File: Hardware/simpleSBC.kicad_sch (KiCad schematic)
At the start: 56 parts, among them J1 Conn_02x07_Odd_Even, J3 Conn_01x06_Male, J5 USB_A, J6 USB_A, J7 RJ45_Wuerth_7499010121A, U1 STM32MP157FAD1, U2 STMPS2252MTR, U5 USBLC6-4SC6, U6 LAN8742A, X1 ASCO, Y1 32.786, Y2 X53T-C20SSA-25.000MHz

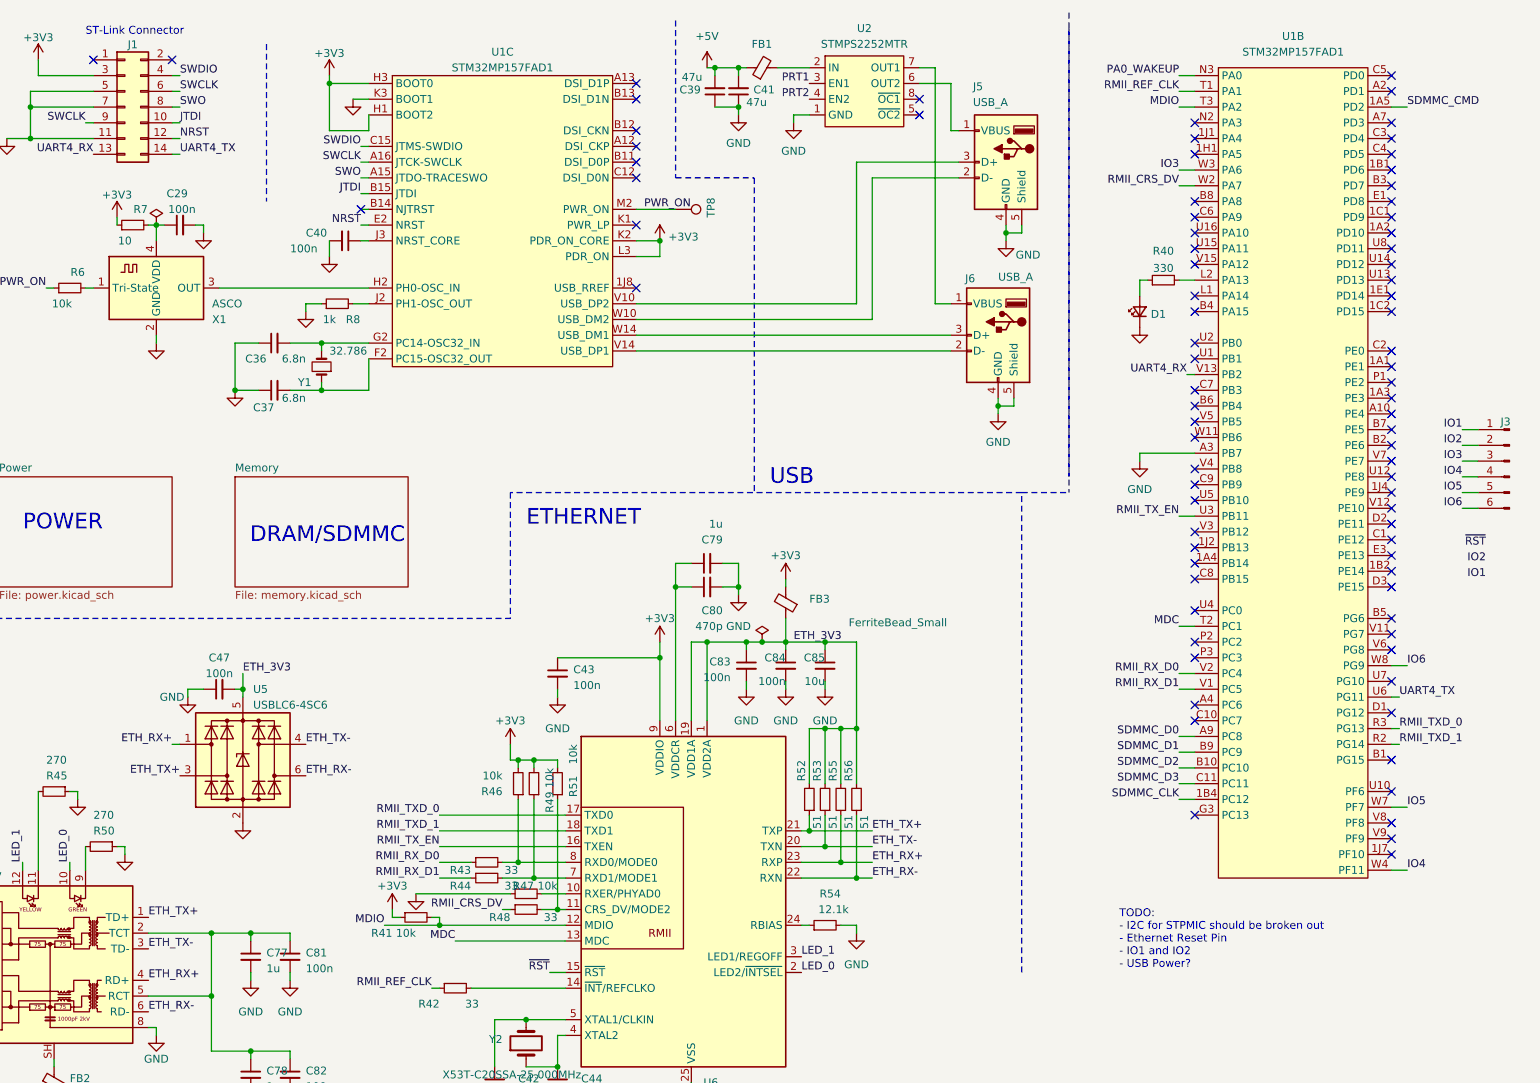
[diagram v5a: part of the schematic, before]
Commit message: Schematic symbol pin type fixes
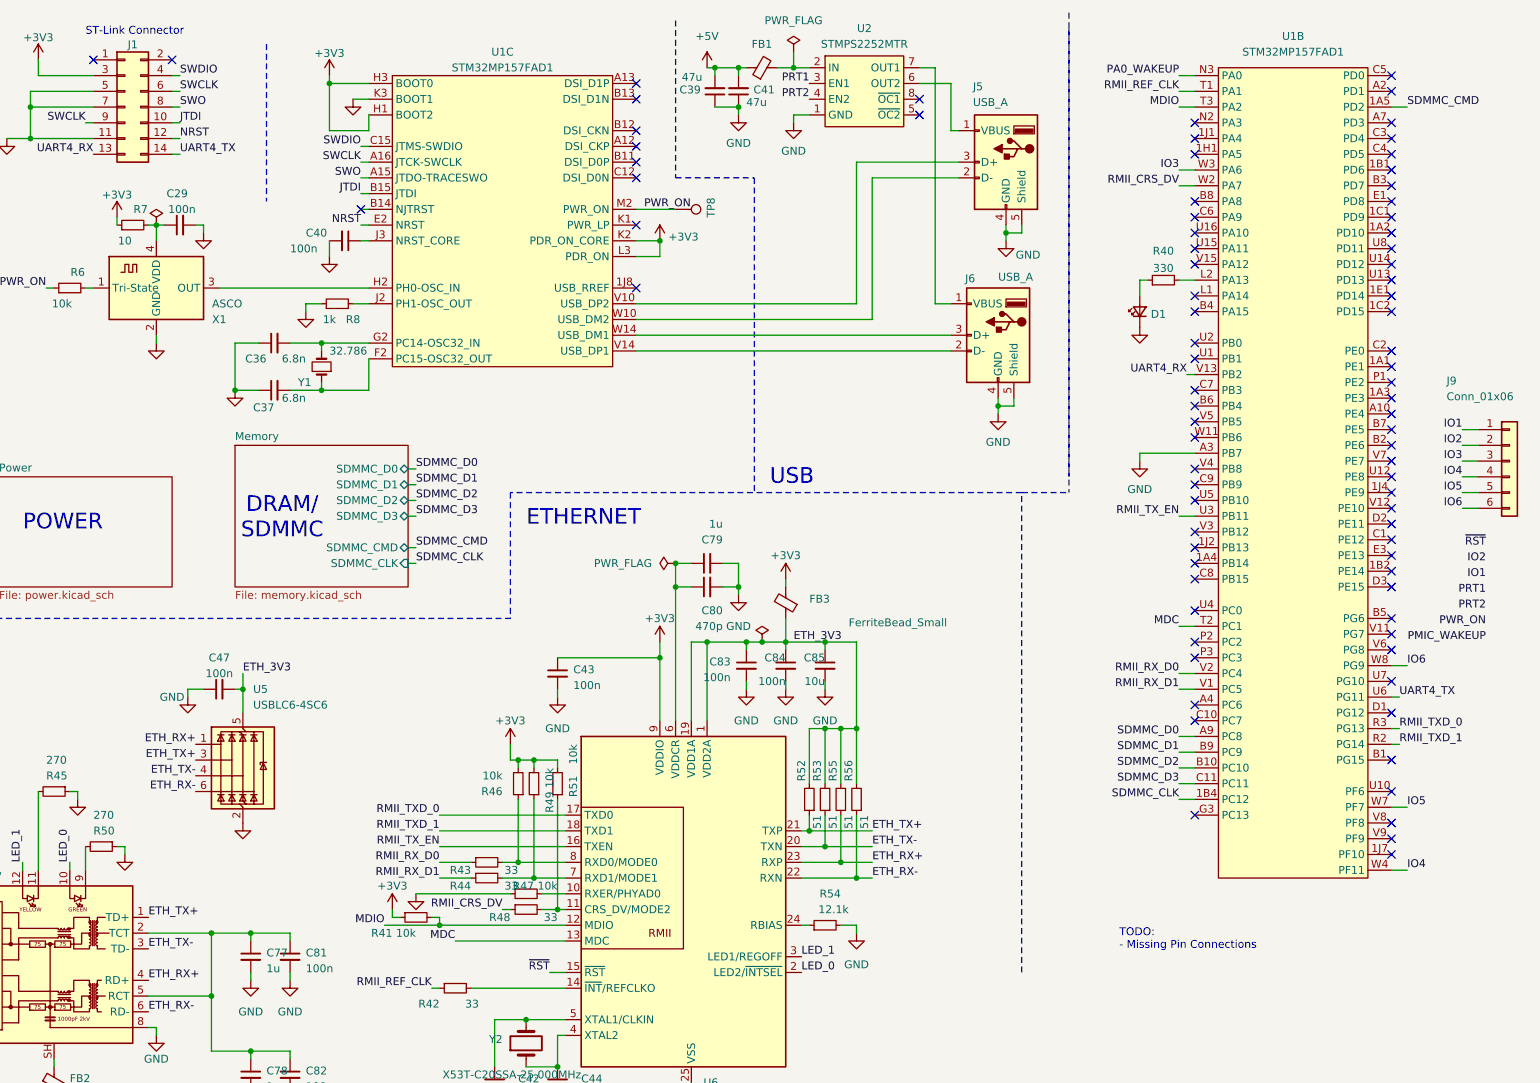
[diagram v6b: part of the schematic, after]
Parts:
- removed J3: Conn_01x06_Male, Connector_PinHeader_2.54mm:PinHeader_1x06_P2.54mm_Vertical, symbol Connector:Conn_01x06_Male
- added J9: Conn_01x06, Connector_PinHeader_2.54mm:PinHeader_1x06_P2.54mm_Vertical, symbol Connector_Generic:Conn_01x06
- FB1: footprint (none) -> Inductor_SMD:L_0603_1608Metric
- J1: footprint personal:PinHeader_2x7_P1.27mm_SMD -> SimpleSBC:PinHeader_2x7_P1.27mm_SMD
- R41, R42, R43, R44, R45, R46, R47, R48, R49, R50, R51, R52, R53, R54, R55, R56: footprint Resistor_SMD:R_0603_1608Metric -> Resistor_SMD:R_0402_1005Metric
- TP8: footprint personal:PROBE_PAD_1206 -> TestPoint:TestPoint_Pad_D1.0mm
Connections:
- net IO1: now also J9.1 (Pin_1)
- net IO2: now also J9.2 (Pin_2)
- net IO3: now also J9.3 (Pin_3)
- net IO4: now also J9.4 (Pin_4)
- net IO5: now also J9.5 (Pin_5)
- net IO6: now also J9.6 (Pin_6)
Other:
- sheet Memory ports: added SDMMC_CLK, SDMMC_CMD, SDMMC_D0, SDMMC_D1, SDMMC_D2, SDMMC_D3; removed none
- note added: "DRAM/ SDMMC"
- note added: "TODO: - Missing Pin Connections"
- note removed: "DRAM/SDMMC"
- note removed: "TODO: - I2C for STPMIC should be broken out - Ethernet Reset Pin - IO1 and IO2 - USB Power?"

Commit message: First pass through ST Design Checklist
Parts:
- removed FB2: FerriteBead_Small, Inductor_SMD:L_0603_1608Metric, symbol Device:FerriteBead_Small
- added C97: 10n, Capacitor_SMD:C_0402_1005Metric, symbol Device:C_Small
- added D2: LED_Small, LED_SMD:LED_0805_2012Metric, symbol Device:LED_Small
- added JP1: SolderJumper_2_Bridged, symbol Jumper:SolderJumper_2_Bridged
- added R60: 10k, Resistor_SMD:R_0402_1005Metric, symbol Device:R_Small
- added R61: 330, Resistor_SMD:R_0402_1005Metric, symbol Device:R_Small
- added R62: 3k, Resistor_SMD:R_0402_1005Metric, symbol Device:R_Small
- C40: value 100n -> 10n
- C42, C43, C44, C47, C77, C78, C79, C80, C81, C82, C83, C84: footprint Capacitor_SMD:C_0603_1608Metric -> Capacitor_SMD:C_0402_1005Metric
- R8: value 1k -> 470
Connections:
- net +3V3: now also C77.1, C78.1, C81.1, C82.1, J7.2 (TCT), J7.5 (RCT), R60.2
- net GND: now also C97.2, D2.1 (K), R62.1
- net NRST: now also C97.1, JP1.2 (B)
- net UART4_RX: now also R60.1
- net ~{RST}: no longer U6.15 (~{RST})
- net RTC_OUT1: now reaches U1.G3 (PC13)
- net at U1.L1 (PA14): now also R61.2
- net I2C4_SDA: now reaches U1.U13 (PD13)
- net I2C4_SCL: now reaches U1.U14 (PD12)
- net at U1.1J8 (USB_RREF): now also R62.2
- new net: D2.2 (A), R61.1
- new net Power/~{RST}: JP1.1 (A)
- no-connect marks 83 -> 80
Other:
- sheet Power ports: added I2C4_SCL, I2C4_SDA, PA0_WAKEUP, PMIC_WAKEUP, PWR_ON, ~{RST}; removed none
- note added: "Route these so they can be severed"
- note added: "TODO: - Missing Pin Connections - What to do with OTG_VBUS (V16) - Disconnect DSI pins? - Check BOOT pin values - Last checkbox pg. 21 - DRAM LDM Question - OTG VBUS? - RJ45 LEDs?"
- note removed: "TODO: - Missing Pin Connections"
- moved on the sheet: D1

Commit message: First Pass for Floorplanning
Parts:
- added JP2, JP3: SolderJumper_2_Bridged, symbol Jumper:SolderJumper_2_Bridged
- added R63: 10k, Resistor_SMD:R_0402_1005Metric, symbol Device:R_Small
- added SW1: SW_Push, symbol Switch:SW_Push
- Y2: footprint Crystal:Crystal_SMD_MicroCrystal_CM9V-T1A-2Pin_1.6x1.0mm -> (none)
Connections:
- net +3V3: now also R63.2
- net GND: now also SW1.1
- net I2C4_SCL: now also JP2.2 (B); no longer U1.U14 (PD12)
- net I2C4_SDA: now also JP3.2 (B); no longer U1.U13 (PD13)
- net NRST: now also R63.1, SW1.2
- net USB_~{OC2}: now reaches U2.5 (~{OC2})
- net USB_~{OC1}: now reaches U2.8 (~{OC1})
- new net: JP2.1 (A), U1.U14 (PD12)
- new net: JP3.1 (A), U1.U13 (PD13)
- no-connect marks 80 -> 78
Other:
- note removed: "Route these so they can be severed"
- moved on the sheet: C29, C39, C41, FB1, J5, J6, R6, R7, U2, X1
